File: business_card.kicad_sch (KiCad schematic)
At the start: 13 parts, among them Q1 2N3904, SW1 SW_SPST, U1 TLC555IP

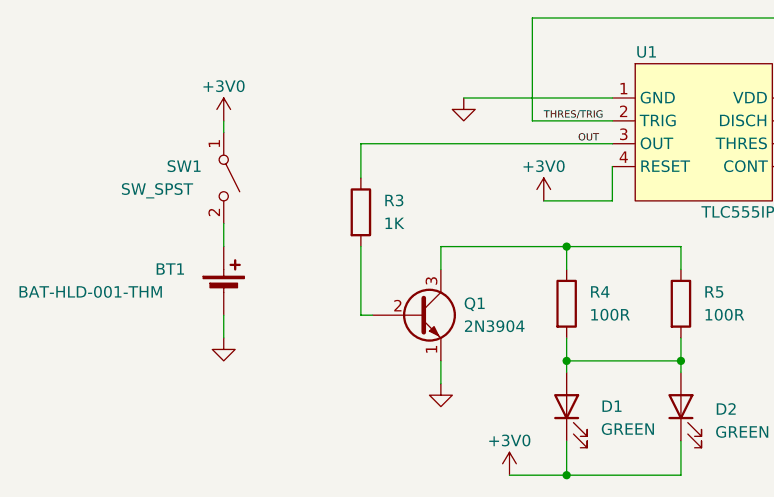
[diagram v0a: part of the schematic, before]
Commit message: Add SPST switch
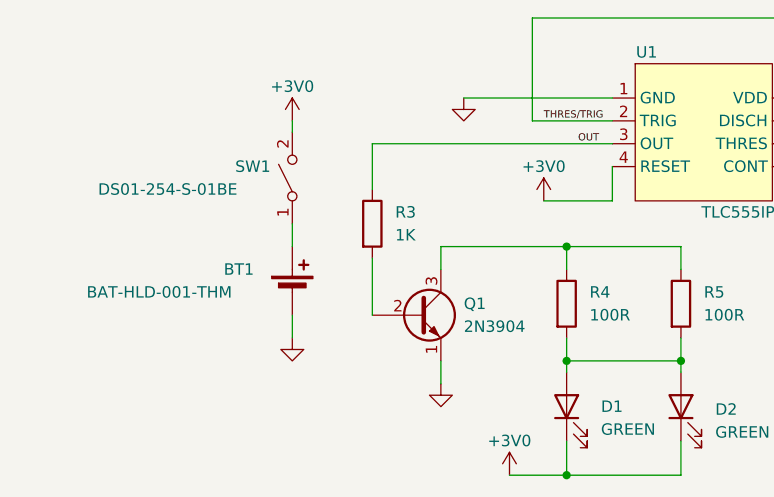
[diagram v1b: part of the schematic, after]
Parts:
- removed SW1: SW_SPST, symbol Switch:SW_SPST
- added SW1: DS01-254-S-01BE, business_card:DS01254S01BE, symbol business_card:DS01-254-S-01BE
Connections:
- net +3V0: now also SW1.2
- net at BT1.1 (+): now also SW1.1
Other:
- moved on the sheet: BT1, R3
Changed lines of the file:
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@@
 	(wire
 		(pts
-			(xy 92.71 111.76) (xy 92.71 114.3)
+			(xy 100.33 111.76) (xy 100.33 114.3)
 		)
 		(stroke
@@
 	(wire
 		(pts
-			(xy 107.95 102.87) (xy 107.95 106.68)
+			(xy 109.22 102.87) (xy 109.22 107.95)
 		)
 		(stroke
@@
 	(wire
 		(pts
-			(xy 92.71 121.92) (xy 92.71 124.46)
+			(xy 100.33 121.92) (xy 100.33 124.46)
 		)
 		(stroke
@@
 	(wire
 		(pts
-			(xy 107.95 102.87) (xy 135.89 102.87)
+			(xy 109.22 102.87) (xy 135.89 102.87)
 		)
 		(stroke
@@
 	(wire
 		(pts
-			(xy 92.71 100.33) (xy 92.71 101.6)
+			(xy 100.33 100.33) (xy 100.33 101.6)
 		)
 		(stroke
@@
 	(wire
 		(pts
-			(xy 107.95 121.92) (xy 109.22 121.92)
-		)
-		(stroke
-			(width 0)
-			(type default)
-		)
-	)
-	(wire
-		(pts
 			(xy 127 100.33) (xy 127 88.9)
 		)
@@
 	(wire
 		(pts
-			(xy 107.95 114.3) (xy 107.95 121.92)
+			(xy 109.22 115.57) (xy 109.22 121.92)
 		)
 		(stroke
@@
 	(symbol
 		(lib_id "power:+3V0")
-		(at 92.71 100.33 0)
+		(at 100.33 100.33 0)
 		(unit 1)
 		(exclude_from_sim no)
@@
 		(dnp no)
 		(property "Reference" "#PWR08"
-			(at 92.71 104.14 0)
+			(at 100.33 104.14 0)
 			(effects
 				(font
@@
 		)
 		(property "Value" "+3V0"
-			(at 92.71 96.52 0)
+			(at 100.33 96.52 0)
 			(effects
 				(font
@@
 		)
 		(property "Footprint" ""
-			(at 92.71 100.33 0)
+			(at 100.33 100.33 0)
 			(effects
 				(font
@@
 		)
 		(property "Datasheet" ""
-			(at 92.71 100.33 0)
+			(at 100.33 100.33 0)
 			(effects
 				(font
@@
 		)
 		(property "Description" "Power symbol creates a global label with name \"+3V0\""
-			(at 92.71 100.33 0)
+			(at 100.33 100.33 0)
 			(effects
 				(font
@@
 		(lib_name "GND_1")
 		(lib_id "power:GND")
-		(at 92.71 124.46 0)
+		(at 100.33 124.46 0)
 		(unit 1)
 		(exclude_from_sim no)
@@
 		(fields_autoplaced yes)
 		(property "Reference" "#PWR09"
-			(at 92.71 130.81 0)
+			(at 100.33 130.81 0)
 			(effects
 				(font
@@
 		)
 		(property "Value" "GND"
-			(at 92.71 129.54 0)
+			(at 100.33 129.54 0)
 			(effects
 				(font
@@
 		)
 		(property "Footprint" ""
-			(at 92.71 124.46 0)
+			(at 100.33 124.46 0)
 			(effects
 				(font
@@
 		)
 		(property "Datasheet" ""
-			(at 92.71 124.46 0)
+			(at 100.33 124.46 0)
 			(effects
 				(font
@@
 		)
 		(property "Description" "Power symbol creates a global label with name \"GND\" , ground"
-			(at 92.71 124.46 0)
+			(at 100.33 124.46 0)
 			(effects
 				(font
@@
 	(symbol
 		(lib_id "Device:R")
-		(at 107.95 110.49 0)
+		(at 109.22 111.76 0)
 		(unit 1)
 		(exclude_from_sim no)
@@
 		(fields_autoplaced yes)
 		(property "Reference" "R3"
-			(at 110.49 109.2199 0)
+			(at 111.76 110.4899 0)
 			(effects
 				(font
@@
 		)
 		(property "Value" "1K"
-			(at 110.49 111.7599 0)
+			(at 111.76 113.0299 0)
 			(effects
 				(font
@@
 		)
 		(property "Footprint" "Resistor_THT:R_Axial_DIN0207_L6.3mm_D2.5mm_P10.16mm_Horizontal"
-			(at 106.172 110.49 90)
+			(at 107.442 111.76 90)
 			(effects
 				(font
@@
 		)
 		(property "Datasheet" "~"
-			(at 107.95 110.49 0)
+			(at 109.22 111.76 0)
 			(effects
 				(font
@@
 		)
 		(property "Description" ""
-			(at 107.95 110.49 0)
+			(at 109.22 111.76 0)
 			(effects
 				(font
@@
 	(symbol
 		(lib_id "Device:Battery_Cell")
-		(at 92.71 119.38 0)
+		(at 100.33 119.38 0)
 		(unit 1)
 		(exclude_from_sim no)
@@
 		(dnp no)
 		(property "Reference" "BT1"
-			(at 85.09 116.84 0)
+			(at 92.71 116.84 0)
 			(effects
 				(font
@@
 		)
 		(property "Value" "BAT-HLD-001-THM"
-			(at 69.85 119.38 0)
+			(at 77.47 119.38 0)
 			(effects
 				(font
@@
 		)
 		(property "Footprint" "business_card:BAT-HLD-001-THM"
-			(at 92.71 117.856 90)
+			(at 100.33 117.856 90)
 			(effects
 				(font
@@
 		)
 		(property "Datasheet" "~https://www.mouser.it/datasheet/2/418/9/ENG_CD_C_BAT_HLD_001_THM_pp_A-3247749.pdf"
-			(at 92.71 117.856 90)
+			(at 100.33 117.856 90)
 			(effects
 				(font
@@
 		)
 		(property "Description" "Single-cell battery"
-			(at 92.71 119.38 0)
+			(at 100.33 119.38 0)
 			(effects
 				(font
@@
 	)
 	(symbol
-		(lib_id "Switch:SW_SPST")
-		(at 92.71 106.68 270)
-		(unit 1)
-		(exclude_from_sim no)
-		(in_bom yes)
-		(on_board yes)
-		(dnp no)
-		(property "Reference" "SW1"
-			(at 86.36 105.41 90)
-			(effects
-				(font
-					(size 1.27 1.27)
-				)
-				(justify left)
-			)
-		)
-		(property "Value" "SW_SPST"
-			(at 81.28 107.95 90)
-			(effects
-				(font
-					(size 1.27 1.27)
-				)
-				(justify left)
-			)
-		)
-		(property "Footprint" ""
-			(at 92.71 106.68 0)
-			(effects
-				(font
-					(size 1.27 1.27)
-				)
-				(hide yes)
-			)
-		)
-		(property "Datasheet" "~"
-			(at 92.71 106.68 0)
-			(effects
-				(font
-					(size 1.27 1.27)
-				)
-				(hide yes)
-			)
-		)
-		(property "Description" "Single Pole Single Throw (SPST) switch"
-			(at 92.71 106.68 0)
-			(effects
-				(font
-					(size 1.27 1.27)
-				)
-				(hide yes)
-			)
-		)
-		(pin "1"
-		)
-		(pin "2"
-		)
-		(instances
-			(project "business_card"
-				(path "/b84feb65-b9c7-4def-9ca7-9e4ec7b305d8"
-					(reference "SW1")
-					(unit 1)
-				)
-			)
-		)
-	)
-	(symbol
 		(lib_id "Device:LED")
 		(at 143.51 132.08 90)
@@
 					(unit 1)
 				)
+			)
+		)
+	)
+	(symbol
+		(lib_id "business_card:DS01-254-S-01BE")
+		(at 100.33 106.68 90)
+		(unit 1)
+		(exclude_from_sim no)
+		(in_bom yes)
+		(on_board yes)
+		(dnp no)
+		(property "Reference" "SW1"
+			(at 93.98 105.41 90)
+			(effects
+				(font
+					(size 1.27 1.27)
+				)
+				(justify right)
+			)
+		)
+		(property "Value" "DS01-254-S-01BE"
+			(at 78.74 107.95 90)
+			(effects
+				(font
+					(size 1.27 1.27)
+				)
+				(justify right)
+			)
+		)
+		(property "Footprint" "business_card:DS01254S01BE"
+			(at 100.33 106.68 0)
+			(effects
+				(font
+					(size 1.27 1.27)
+				)
+				(hide yes)
+			)
+		)
+		(property "Datasheet" "https://www.mouser.it/datasheet/2/670/ds01_254-1777712.pdf"
+			(at 100.33 106.68 0)
+			(effects
+				(font
+					(size 1.27 1.27)
+				)
+				(hide yes)
+			)
+		)
+		(property "Description" ""
+			(at 100.33 106.68 0)
+			(effects
+				(font
+					(size 1.27 1.27)
+				)
+				(hide yes)
+			)
+		)
+		(pin "2"
+		)
+		(pin "1"
+		)
+		(instances
+			(project "business_card"
+				(path "/b84feb65-b9c7-4def-9ca7-9e4ec7b305d8"
+					(reference "SW1")
+					(unit 1)
+				)

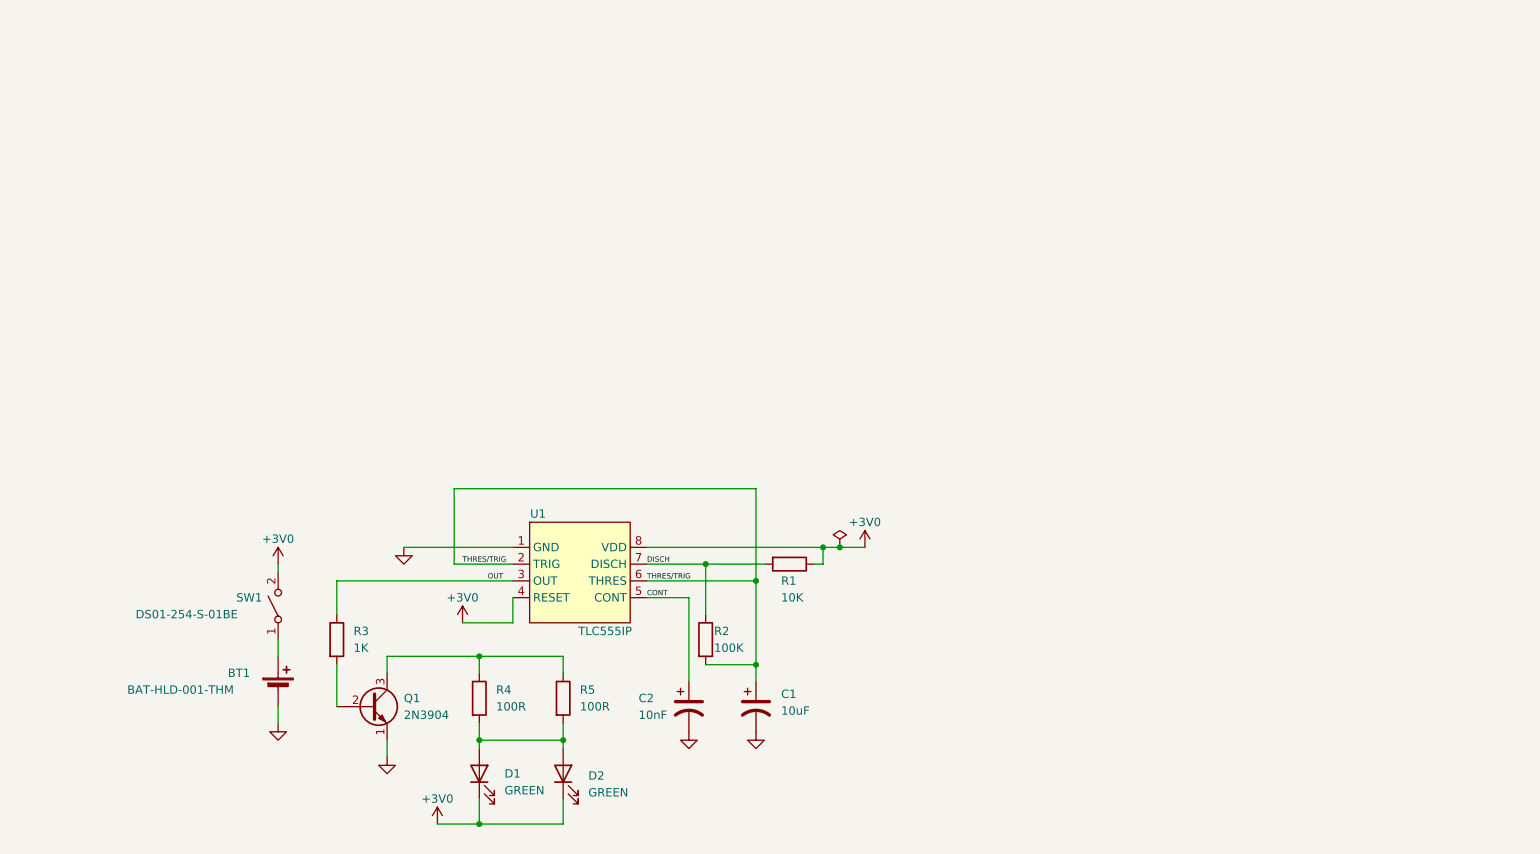
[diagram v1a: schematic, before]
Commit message: Add potentiometer and update switch footprint
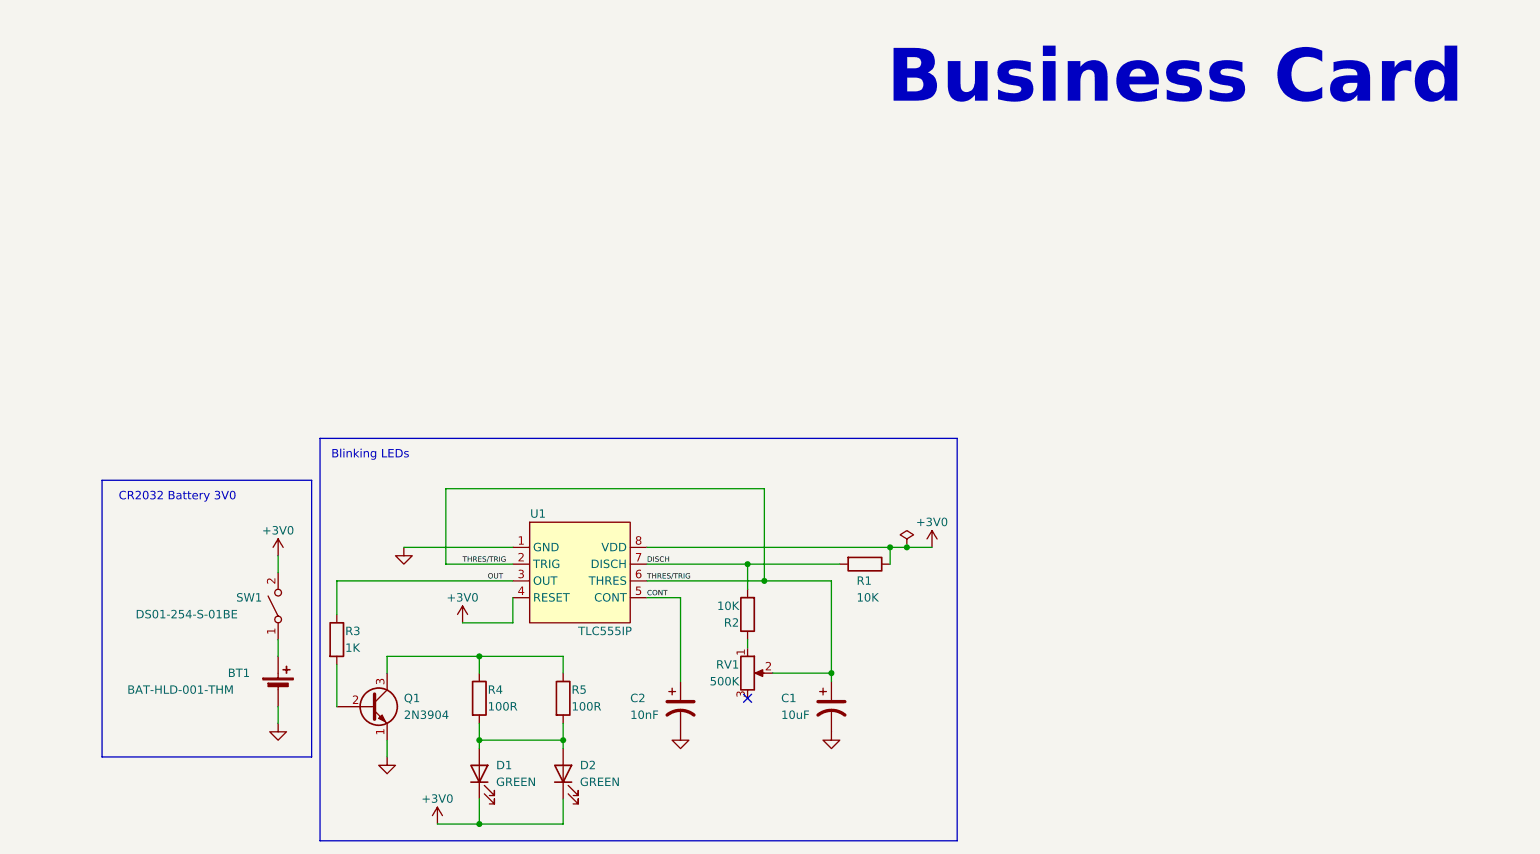
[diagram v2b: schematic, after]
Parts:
- added RV1: 500K, business_card:3306P-1-504, symbol Device:R_Potentiometer
- R2: value 100K -> 10K
- SW1: footprint business_card:DS01254S01BE -> business_card:DS01-254-S-01BE
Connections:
- net DISCH: now also R2.2; no longer R2.1
- net THRES/TRIG: now also RV1.2; no longer R2.2
- new net: R2.1, RV1.1
- no-connect marks 0 -> 1
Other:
- note added: "Blinking LEDs"
- note added: "Business Card"
- note added: "CR2032 Battery 3V0"
- moved on the sheet: C1, C2, R1, R2

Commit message: Update PCB layout
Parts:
- SW1: footprint business_card:DS01-254-S-01BE -> business_card:DS01254S01BE
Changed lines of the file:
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@@
 			)
 		)
-		(property "Footprint" "business_card:DS01-254-S-01BE"
+		(property "Footprint" "business_card:DS01254S01BE"
 			(at 100.33 106.68 0)
 			(effects

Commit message: Add traces and Replace 2N3904 footprint
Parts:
- Q1: footprint Package_TO_SOT_THT:TO-92_Inline -> business_card:2N3904
- SW1: footprint business_card:DS01254S01BE -> business_card:DS01-254-S-01BE
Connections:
- net GND: now also BT1.1 (-); no longer BT1.2 (-)
- net at SW1.1: now also BT1.2 (+); no longer BT1.1 (+)
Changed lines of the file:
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@@
 			)
 		)
-		(property "Footprint" "Package_TO_SOT_THT:TO-92_Inline"
+		(property "Footprint" "business_card:2N3904"
 			(at 119.38 123.825 0)
 			(effects
@@
 			)
 		)
-		(property "Datasheet" "https://www.mouser.it/datasheet/2/418/9/ENG_CD_C_BAT_HLD_001_THM_pp_A-3247749.pdf"
+		(property "Datasheet" "~"
 			(at 100.33 117.856 90)
 			(effects
@@
 			)
 		)
-		(property "Footprint" "business_card:DS01254S01BE"
+		(property "Footprint" "business_card:DS01-254-S-01BE"
 			(at 100.33 106.68 0)
 			(effects

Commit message: Make the board ready for manufacturing! :)
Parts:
- removed BT1: BAT-HLD-001-THM, business_card:BAT-HLD-001-THM, symbol Device:Battery_Cell
- added BT1: BAT-HLD-001-THM, business_card:BAT-HLD-001-THM, symbol business_card:BAT-HLD-001-THM
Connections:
- net GND: now also BT1.1 (GND)
- net at SW1.1: now also BT1.2 (+3V0), BT1.3 (+3V0), BT1.4 (+3V0), BT1.5 (+3V0)
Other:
- note added: "CR2032 Battery +3V0"
- note removed: "CR2032 Battery 3V0"
- moved on the sheet: SW1
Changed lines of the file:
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@@
+	)
+	(junction
+		(at 96.52 118.11)
+		(diameter 0)
+		(color 0 0 0 0)
+	)
+	(junction
+		(at 96.52 123.19)
+		(diameter 0)
+		(color 0 0 0 0)
 	)
 	(junction
@@
 	)
 	(junction
+		(at 96.52 120.65)
+		(diameter 0)
+		(color 0 0 0 0)
+	)
+	(junction
 		(at 195.58 97.79)
 		(diameter 0)
@@
 	(wire
 		(pts
+			(xy 92.71 120.65) (xy 96.52 120.65)
+		)
+		(stroke
+			(width 0)
+			(type default)
+		)
+	)
+	(wire
+		(pts
+			(xy 92.71 125.73) (xy 96.52 125.73)
+		)
+		(stroke
+			(width 0)
+			(type default)
+		)
+	)
+	(wire
+		(pts
 			(xy 125.73 88.9) (xy 173.99 88.9)
 		)
@@
 	(wire
 		(pts
-			(xy 100.33 111.76) (xy 100.33 114.3)
-		)
-		(stroke
-			(width 0)
-			(type default)
-		)
-	)
-	(wire
-		(pts
 			(xy 130.81 139.7) (xy 143.51 139.7)
 		)
@@
 	(wire
 		(pts
+			(xy 92.71 123.19) (xy 96.52 123.19)
+		)
+		(stroke
+			(width 0)
+			(type default)
+		)
+	)
+	(wire
+		(pts
 			(xy 116.84 114.3) (xy 130.81 114.3)
 		)
@@
 	(wire
 		(pts
-			(xy 100.33 121.92) (xy 100.33 124.46)
+			(xy 96.52 118.11) (xy 96.52 110.49)
 		)
 		(stroke
@@
 	(wire
 		(pts
+			(xy 96.52 123.19) (xy 96.52 120.65)
+		)
+		(stroke
+			(width 0)
+			(type default)
+		)
+	)
+	(wire
+		(pts
+			(xy 96.52 120.65) (xy 96.52 118.11)
+		)
+		(stroke
+			(width 0)
+			(type default)
+		)
+	)
+	(wire
+		(pts
 			(xy 116.84 127) (xy 116.84 129.54)
 		)
@@
 	(wire
 		(pts
+			(xy 73.66 121.92) (xy 66.04 121.92)
+		)
+		(stroke
+			(width 0)
+			(type default)
+		)
+	)
+	(wire
+		(pts
 			(xy 143.51 114.3) (xy 143.51 116.84)
 		)
@@
 	(wire
 		(pts
+			(xy 92.71 118.11) (xy 96.52 118.11)
+		)
+		(stroke
+			(width 0)
+			(type default)
+		)
+	)
+	(wire
+		(pts
 			(xy 109.22 102.87) (xy 135.89 102.87)
 		)
@@
 	(wire
 		(pts
-			(xy 100.33 99.06) (xy 100.33 101.6)
+			(xy 96.52 125.73) (xy 96.52 123.19)
 		)
 		(stroke
@@
 	(wire
 		(pts
+			(xy 96.52 96.52) (xy 96.52 100.33)
+		)
+		(stroke
+			(width 0)
+			(type default)
+		)
+	)
+	(wire
+		(pts
 			(xy 195.58 97.79) (xy 199.39 97.79)
 		)
@@
 		(pts
 			(xy 124.46 139.7) (xy 130.81 139.7)
+		)
+		(stroke
+			(width 0)
+			(type default)
+		)
+	)
+	(wire
+		(pts
+			(xy 66.04 121.92) (xy 66.04 127)
 		)
 		(stroke
@@
 	)
 	(rectangle
-		(start 73.66 87.63)
-		(end 105.41 129.54)
+		(start 60.96 86.36)
+		(end 101.6 138.43)
 		(stroke
 			(width 0)
@@
 	(text "Business Card"
 		(exclude_from_sim no)
-		(at 236.22 26.67 0)
+		(at 237.49 25.4 0)
 		(effects
 			(font
@@
 		)
 	)
-	(text "CR2032 Battery 3V0"
-		(exclude_from_sim no)
-		(at 85.09 90.17 0)
+	(text "CR2032 Battery +3V0"
+		(exclude_from_sim no)
+		(at 72.39 88.9 0)
 		(effects
 			(font
@@
 	)
 	(symbol
+		(lib_id "business_card:BAT-HLD-001-THM")
+		(at 82.55 121.92 0)
+		(unit 1)
+		(exclude_from_sim no)
+		(in_bom yes)
+		(on_board yes)
+		(dnp no)
+		(property "Reference" "BT1"
+			(at 83.185 132.08 0)
+			(effects
+				(font
+					(size 1.27 1.27)
+				)
+			)
+		)
+		(property "Value" "BAT-HLD-001-THM"
+			(at 83.185 129.54 0)
+			(effects
+				(font
+					(size 1.27 1.27)
+				)
+			)
+		)
+		(property "Footprint" "business_card:BAT-HLD-001-THM"
+			(at 82.55 121.92 0)
+			(effects
+				(font
+					(size 1.27 1.27)
+				)
+				(hide yes)
+			)
+		)
+		(property "Datasheet" "https://www.mouser.it/datasheet/2/418/9/ENG_CD_C_BAT_HLD_001_THM_pp_A-3247749.pdf"
+			(at 82.55 121.92 0)
+			(effects
+				(font
+					(size 1.27 1.27)
+				)
+				(hide yes)
+			)
+		)
+		(property "Description" ""
+			(at 82.55 121.92 0)
+			(effects
+				(font
+					(size 1.27 1.27)
+				)
+				(hide yes)
+			)
+		)
+		(pin "3"
+		)
+		(pin "1"
+		)
+		(pin "2"
+		)
+		(pin "4"
+		)
+		(pin "5"
+		)
+		(instances
+			(project ""
+				(path "/b84feb65-b9c7-4def-9ca7-9e4ec7b305d8"
+					(reference "BT1")
+					(unit 1)
+				)
+			)
+		)
+	)
+	(symbol
 		(lib_id "power:PWR_FLAG")
 		(at 195.58 97.79 0)
@@
 	(symbol
 		(lib_id "power:+3V0")
-		(at 100.33 99.06 0)
+		(at 96.52 96.52 0)
 		(unit 1)
 		(exclude_from_sim no)
@@
 		(dnp no)
 		(property "Reference" "#PWR08"
-			(at 100.33 102.87 0)
+			(at 96.52 100.33 0)
 			(effects
 				(font
@@
 		)
 		(property "Value" "+3V0"
-			(at 100.33 95.25 0)
+			(at 96.52 92.71 0)
 			(effects
 				(font
@@
 		)
 		(property "Footprint" ""
-			(at 100.33 99.06 0)
+			(at 96.52 96.52 0)
 			(effects
 				(font
@@
 		)
 		(property "Datasheet" ""
-			(at 100.33 99.06 0)
+			(at 96.52 96.52 0)
 			(effects
 				(font
@@
 		)
 		(property "Description" "Power symbol creates a global label with name \"+3V0\""
-			(at 100.33 99.06 0)
+			(at 96.52 96.52 0)
 			(effects
 				(font
@@
 		(lib_name "GND_1")
 		(lib_id "power:GND")
-		(at 100.33 124.46 0)
+		(at 66.04 127 0)
 		(unit 1)
 		(exclude_from_sim no)
@@
 		(fields_autoplaced yes)
 		(property "Reference" "#PWR09"
-			(at 100.33 130.81 0)
+			(at 66.04 133.35 0)
 			(effects
 				(font
@@
 		)
 		(property "Value" "GND"
-			(at 100.33 129.54 0)
+			(at 66.04 132.08 0)
 			(effects
 				(font
@@
 		)
 		(property "Footprint" ""
-			(at 100.33 124.46 0)
+			(at 66.04 127 0)
 			(effects
 				(font
@@
 		)
 		(property "Datasheet" ""
-			(at 100.33 124.46 0)
+			(at 66.04 127 0)
 			(effects
 				(font
@@
 		)
 		(property "Description" "Power symbol creates a global label with name \"GND\" , ground"
-			(at 100.33 124.46 0)
+			(at 66.04 127 0)
 			(effects
 				(font
@@
 	)
 	(symbol
-		(lib_id "Device:Battery_Cell")
-		(at 100.33 119.38 0)
-		(unit 1)
-		(exclude_from_sim no)
-		(in_bom yes)
-		(on_board yes)
-		(dnp no)
-		(property "Reference" "BT1"
-			(at 92.71 116.84 0)
-			(effects
-				(font
-					(size 1.27 1.27)
-				)
-				(justify left)
-			)
-		)
-		(property "Value" "BAT-HLD-001-THM"
-			(at 77.47 119.38 0)
-			(effects
-				(font
-					(size 1.27 1.27)
-				)
-				(justify left)
-			)
-		)
-		(property "Footprint" "business_card:BAT-HLD-001-THM"
-			(at 100.33 117.856 90)
-			(effects
-				(font
-					(size 1.27 1.27)
-				)
-				(hide yes)
-			)
-		)
-		(property "Datasheet" "~"
-			(at 100.33 117.856 90)
-			(effects
-				(font
-					(size 1.27 1.27)
-				)
-				(hide yes)
-			)
-		)
-		(property "Description" "Single-cell battery"
-			(at 100.33 119.38 0)
-			(effects
-				(font
-					(size 1.27 1.27)
-				)
-				(hide yes)
-			)
-		)
-		(pin "2"
-		)
-		(pin "1"
-		)
-		(instances
-			(project "business_card"
-				(path "/b84feb65-b9c7-4def-9ca7-9e4ec7b305d8"
-					(reference "BT1")
-					(unit 1)
-				)
-			)
-		)
-	)
-	(symbol
 		(lib_id "power:+3V0")
 		(at 124.46 139.7 0)
@@
 	(symbol
 		(lib_id "business_card:DS01-254-S-01BE")
-		(at 100.33 106.68 90)
+		(at 96.52 105.41 90)
 		(unit 1)
 		(exclude_from_sim no)
@@
 		(dnp no)
 		(property "Reference" "SW1"
-			(at 93.98 105.41 90)
+			(at 90.17 104.14 90)
 			(effects
 				(font
@@
 		)
 		(property "Value" "DS01-254-S-01BE"
-			(at 78.74 107.95 90)
+			(at 74.93 106.68 90)
 			(effects
 				(font
@@
 		)
 		(property "Footprint" "business_card:DS01-254-S-01BE"
-			(at 100.33 106.68 0)
+			(at 96.52 105.41 0)
 			(effects
 				(font
@@
 		)
 		(property "Datasheet" "https://www.mouser.it/datasheet/2/670/ds01_254-1777712.pdf"
-			(at 100.33 106.68 0)
+			(at 96.52 105.41 0)
 			(effects
 				(font
@@
 		)
 		(property "Description" ""
-			(at 100.33 106.68 0)
-			(effects
-				(font
+			(at 96.52 105.41 0)
+			(effects
+				(font
